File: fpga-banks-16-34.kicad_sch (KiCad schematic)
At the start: 25 parts, among them U1 ASFLMB-100.000MHZ-XY-T, U15 XC7K160T-FFG676, U8 PCA9517ADMR2G

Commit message: Rebase to Rev. 1.2.2
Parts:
- removed C145, C146, C18, C206, C207: C_100n_0402, antmicro-footprints:0402-cap, symbol antmicroCapacitors0402:C_100n_0402
- removed R163: R_10k_0402, data-center-dram-tester-footprints:0402-res, symbol data-center-dram-tester:R_10k_0402
- removed R164, R165, R166, R167, R168, R169: R_0R_0402, data-center-dram-tester-footprints:0402-res, symbol data-center-dram-tester:R_0R_0402
- removed R170, R171, R172, R173, R174: R_4k7_0402, data-center-dram-tester-footprints:0402-res, symbol data-center-dram-tester:R_4k7_0402
- removed R63, R64: R_80R6_0603, antmicro-footprints:0603-res, symbol antmicroResistors0603:R_80R6_0603
- removed R65, R66: R_1k_0603, data-center-dram-tester-footprints:0603-res, symbol data-center-dram-tester:R_1k_0603
- removed TP12: TP_SMD1MM, data-center-dram-tester-footprints:Testpoint_smd_1mm, symbol data-center-dram-tester:TP_SMD1MM
- removed U1: ASFLMB-100.000MHZ-XY-T, data-center-dram-tester-footprints:ASFLMB-100.000MHZ-XY-T, symbol data-center-dram-tester:ASFLMB-100.000MHZ-XY-T
- removed U15: XC7K160T-FFG676, antmicro-footprints:xc7k160tfbg676, symbol data-center-dram-tester:XC7K160T-FFG676
- removed U8: PCA9517ADMR2G, data-center-dram-tester-footprints:TSSOP-8_W3mm, symbol data-center-dram-tester:PCA9517ADMR2G
- added C145, C146, C18, C206, C207: C_100n_0402, data-center-rdimm-ddr4-tester-footprints:C_0402_1005Metric, symbol data-center-rdimm-ddr4-tester:C_100n_0402
- added R163: R_10k_0402, data-center-rdimm-ddr4-tester-footprints:R_0402_1005Metric, symbol data-center-rdimm-ddr4-tester:R_10k_0402
- added R164, R165, R166, R167, R168, R169: R_0R_0402, data-center-rdimm-ddr4-tester-footprints:R_0402_1005Metric, symbol data-center-rdimm-ddr4-tester:R_0R_0402
- added R170, R171, R172, R173, R174: R_4k7_0402, data-center-rdimm-ddr4-tester-footprints:R_0402_1005Metric, symbol data-center-rdimm-ddr4-tester:R_4k7_0402
- added R63, R64: R_80R6_0603, data-center-rdimm-ddr4-tester-footprints:R_0603_1608Metric, symbol data-center-rdimm-ddr4-tester:R_80R6_0603
- added R65, R66: R_1k_0603, data-center-rdimm-ddr4-tester-footprints:R_0603_1608Metric, symbol data-center-rdimm-ddr4-tester:R_1k_0603
- added TP12: TP_1mm_SMD, data-center-rdimm-ddr4-tester-footprints:Testpoint_smd_1mm, symbol data-center-rdimm-ddr4-tester:TP_1mm_SMD
- added U1: Oscillator_SMD_100MHz_ASFLMB, data-center-rdimm-ddr4-tester-footprints:Oscillator_SMD_Abracon_ASFLMB_5x3.2x0.85mm, symbol data-center-rdimm-ddr4-tester:Oscillator_SMD_100MHz_ASFLMB
- added U15: XC7K160T-FFG676, data-center-rdimm-ddr4-tester-footprints:BGA-676_27x27mm_Layout26x26_P1X1mm, symbol data-center-rdimm-ddr4-tester:XC7K160T-FFG676
- added U8: PCA9517A_TSSOP, data-center-rdimm-ddr4-tester-footprints:TSSOP-8_3x3mm_P0.65mm, symbol data-center-rdimm-ddr4-tester:PCA9517A_TSSOP
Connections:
- net 3V3_SYS: now also C145.1, C206.1, R171.1, R172.1, U1.1 (~{STDB}), U1.4 (V_{DD}), U15.A11 (VCCO_16), U15.B8 (VCCO_16), U15.C15 (VCCO_16), U15.D12 (VCCO_16), U15.E9 (VCCO_16), U15.G13 (VCCO_16), U15.H10 (VCCO_16), U8.8 (VREF_{2})
- net A0: now also U15.AF10 (IO_L24P_T3_33)
- net A1: now also U15.AC11 (IO_L13N_T2_MRCC_33)
- net A10\AP: now also U15.Y12 (IO_L18N_T2_33)
- net A11: now also U15.AB7 (IO_L10P_T1_33)
- net A12\~{BC}: now also U15.AC7 (IO_L10N_T1_33)
- net A13: now also U15.AD13 (IO_L17N_T2_33)
- net A17: now also U15.AC13 (IO_L17P_T2_33)
- net A2: now also U15.AD11 (IO_L19P_T3_33)
- net A3: now also U15.AD10 (IO_L20P_T3_33)
- net A4: now also U15.AC9 (IO_L12P_T1_MRCC_33)
- net A5: now also U15.AD9 (IO_L12N_T1_MRCC_33)
- net A6: now also U15.AB9 (IO_L11N_T1_SRCC_33)
- net A7: now also U15.AF7 (IO_L7N_T1_33)
- net A8: now also U15.AE8 (IO_L22P_T3_33)
- net A9: now also U15.AE7 (IO_L7P_T1_33)
- net BA0: now also U15.AB11 (IO_L13P_T2_MRCC_33)
- net BA1: now also U15.AB10 (IO_L14N_T2_SRCC_33)
- net BG0: now also U15.AA9 (IO_L11P_T1_SRCC_33)
- net BG1: now also U15.AF9 (IO_L24N_T3_33)
- net CK0_N: now also U15.AF12 (IO_L21N_T3_DQS_33)
- net CK0_P: now also U15.AE12 (IO_L21P_T3_DQS_33)
- net CK1_N: now also U15.AC12 (IO_L15N_T2_DQS_33)
- net CK1_P: now also U15.AB12 (IO_L15P_T2_DQS_33)
- net CKE0: now also U15.AA8 (IO_L8P_T1_33)
- net CKE1\NC: now also U15.AA7 (IO_L8N_T1_33)
- net DQ0: now also U15.U5 (IO_L1N_T0_34)
- net DQ1: now also U15.V6 (IO_L5N_T0_34)
- net DQ10: now also U15.AC3 (IO_L14N_T2_SRCC_34)
- net DQ11: now also U15.AC4 (IO_L14P_T2_SRCC_34)
- net DQ12: now also U15.W4 (IO_L6N_T0_VREF_34)
- net DQ13: now also U15.V4 (IO_L6P_T0_34)
- net DQ14: now also U15.AA4 (IO_L13P_T2_MRCC_34)
- net DQ15: now also U15.AB4 (IO_L13N_T2_MRCC_34)
- net DQ16: now also U15.V1 (IO_L8N_T1_34)
- net DQ17: now also U15.Y2 (IO_L7N_T1_34)
- net DQ18: now also U15.AC2 (IO_L11N_T1_SRCC_34)
- net DQ19: now also U15.AE1 (IO_L20N_T3_34)
- net DQ2: now also U15.AB6 (IO_L16P_T2_34)
- net DQ20: now also U15.U1 (IO_L2N_T0_34)
- net DQ21: now also U15.V2 (IO_L8P_T1_34)
- net DQ22: now also U15.AB2 (IO_L11P_T1_SRCC_34)
- net DQ23: now also U15.AD1 (IO_L20P_T3_34)
- net DQ24: now also U15.AE3 (IO_L22P_T3_34)
- net DQ25: now also U15.AF3 (IO_L24P_T3_34)
- net DQ26: now also U15.AD5 (IO_L18N_T2_34)
- net DQ27: now also U15.AD6 (IO_L18P_T2_34)
- net DQ28: now also U15.AE2 (IO_L22N_T3_34)
- net DQ29: now also U15.AF2 (IO_L24N_T3_34)
- net DQ3: now also U15.AC6 (IO_L16N_T2_34)
- net DQ30: now also U15.AE5 (IO_L23N_T3_34)
- net DQ31: now also U15.AE6 (IO_L23P_T3_34)
- net DQ32: now also U15.AF15 (IO_L2N_T0_32)
- net DQ33: now also U15.AE16 (IO_L6N_T0_VREF_32)
- net DQ34: now also U15.AF19 (IO_L5P_T0_32)
- net DQ35: now also U15.AF20 (IO_L5N_T0_32)
- net DQ36: now also U15.AF14 (IO_L2P_T0_32)
- net DQ37: now also U15.AD14 (IO_L8N_T1_32)
- net DQ38: now also U15.AF18 (IO_L3N_T0_DQS_32)
- net DQ39: now also U15.AE18 (IO_L3P_T0_DQS_32)
- net DQ4: now also U15.U7 (IO_L5P_T0_34)
- net DQ40: now also U15.AB14 (IO_L10P_T1_32)
- net DQ41: now also U15.AD19 (IO_L17N_T2_32)
- net DQ42: now also U15.AC16 (IO_L12N_T1_MRCC_32)
- net DQ43: now also U15.AB15 (IO_L10N_T1_32)
- net DQ44: now also U15.AC14 (IO_L8P_T1_32)
- net DQ45: now also U15.AD16 (IO_L6P_T0_32)
- net DQ46: now also U15.AC19 (IO_L17P_T2_32)
- net DQ47: now also U15.AC17 (IO_L14N_T2_SRCC_32)
- net DQ48: now also U15.AA15 (IO_L7N_T1_32)
- net DQ49: now also U15.AB17 (IO_L14P_T2_SRCC_32)
- net DQ5: now also U15.U6 (IO_L1P_T0_34)
- net DQ50: now also U15.AA19 (IO_L16P_T2_32)
- net DQ51: now also U15.AA20 (IO_L16N_T2_32)
- net DQ52: now also U15.AA14 (IO_L7P_T1_32)
- net DQ53: now also U15.AB16 (IO_L12P_T1_MRCC_32)
- net DQ54: now also U15.AB19 (IO_L18P_T2_32)
- net DQ55: now also U15.AB20 (IO_L18N_T2_32)
- net DQ56: now also U15.V14 (IO_L24P_T3_32)
- net DQ57: now also U15.Y16 (IO_L9N_T1_DQS_32)
- net DQ58: now also U15.W19 (IO_L21N_T3_DQS_32)
- net DQ59: now also U15.V19 (IO_L23N_T3_32)
- net DQ6: now also U15.AA5 (IO_L15P_T2_DQS_34)
- net DQ60: now also U15.W14 (IO_L24N_T3_32)
- net DQ61: now also U15.Y15 (IO_L9P_T1_DQS_32)
- net DQ62: now also U15.W18 (IO_L21P_T3_DQS_32)
- net DQ63: now also U15.V18 (IO_L23P_T3_32)
- net DQ7: now also U15.AB5 (IO_L15N_T2_DQS_34)
- net DQ8: now also U15.U2 (IO_L2P_T0_34)
- net DQ9: now also U15.Y3 (IO_L7P_T1_34)
- net DQS0_N: now also U15.Y5 (IO_L17N_T2_34)
- net DQS0_P: now also U15.Y6 (IO_L17P_T2_34)
- net DQS10_N: now also U15.W3 (IO_L4N_T0_34)
- net DQS10_P: now also U15.V3 (IO_L4P_T0_34)
- net DQS11_N: now also U15.Y1 (IO_L10N_T1_34)
- net DQS11_P: now also U15.W1 (IO_L10P_T1_34)
- net DQS12_N: now also U15.AD3 (IO_L19N_T3_VREF_34)
- net DQS12_P: now also U15.AD4 (IO_L19P_T3_34)
- net DQS13_N: now also U15.AE15 (IO_L4N_T0_32)
- net DQS13_P: now also U15.AD15 (IO_L4P_T0_32)
- net DQS14_N: now also U15.AE20 (IO_L15N_T2_DQS_32)
- net DQS14_P: now also U15.AD20 (IO_L15P_T2_DQS_32)
- net DQS15_N: now also U15.AA18 (IO_L11N_T1_SRCC_32)
- net DQS15_P: now also U15.AA17 (IO_L11P_T1_SRCC_32)
- net DQS16_N: now also U15.W16 (IO_L22N_T3_32)
- net DQS16_P: now also U15.W15 (IO_L22P_T3_32)
- net DQS1_N: now also U15.AA2 (IO_L12N_T1_MRCC_34)
- net DQS1_P: now also U15.AA3 (IO_L12P_T1_MRCC_34)
- net DQS2_N: now also U15.AC1 (IO_L9N_T1_DQS_34)
- net DQS2_P: now also U15.AB1 (IO_L9P_T1_DQS_34)
- net DQS3_N: now also U15.AF4 (IO_L21N_T3_DQS_34)
- net DQS3_P: now also U15.AF5 (IO_L21P_T3_DQS_34)
- net DQS4_N: now also U15.AF17 (IO_L1N_T0_32)
- net DQS4_P: now also U15.AE17 (IO_L1P_T0_32)
- net DQS5_N: now also U15.AD18 (IO_L13N_T2_MRCC_32)
- net DQS5_P: now also U15.AC18 (IO_L13P_T2_MRCC_32)
- net DQS6_N: now also U15.Y18 (IO_L19N_T3_VREF_32)
- net DQS6_P: now also U15.Y17 (IO_L19P_T3_32)
- net DQS7_N: now also U15.V17 (IO_L20N_T3_32)
- net DQS7_P: now also U15.V16 (IO_L20P_T3_32)
- net DQS9_N: now also U15.W5 (IO_L3N_T0_DQS_34)
- net DQS9_P: now also U15.W6 (IO_L3P_T0_DQS_34)
- net GCLK100: now also U1.3 (OUT), U15.C12 (IO_L13P_T2_MRCC_16)
- net GND: now also C145.2, C146.2, C18.2, C206.2, C207.2, R165.2, R167.2, R169.2, R64.2, R66.2, U1.2 (GND), U8.4 (GND)
- net NC\C2: now also U15.W10 (IO_L3P_T0_DQS_33)
- net ODT0: now also U15.Y13 (IO_L18P_T2_33)
- net ODT1\NC: now also U15.W9 (IO_L3N_T0_DQS_33)
- net PARITY: now also U15.AE13 (IO_L23P_T3_33)
- net SA0: now also R168.2, R169.1
- net SA1: now also R166.2, R167.1
- net SA2: now also R164.2, R165.1
- net SCL_2V5: now also R174.2, U8.2 (SCL_{1})
- net SCL_3V3: now also R171.2, U8.7 (SCL_{2})
- net SDA_2V5: now also R173.2, U8.3 (SDA_{1})
- net SDA_3V3: now also R172.2, U8.6 (SDA_{2})
- net SD_CD: now also U15.F9 (IO_L7P_T1_16)
- net SD_CLK: now also U15.D10 (IO_L12N_T1_MRCC_16)
- net SD_CMD: now also U15.D8 (IO_L8N_T1_16)
- net SD_DAT0: now also U15.E10 (IO_L12P_T1_MRCC_16)
- net SD_DAT1: now also U15.F8 (IO_L7N_T1_16)
- net SD_DAT2: now also U15.C9 (IO_L10P_T1_16)
- net SD_DAT3: now also U15.D9 (IO_L8P_T1_16)
- net TMDS_CLK_N: now also U15.A15 (IO_L23N_T3_16)
- net TMDS_CLK_P: now also U15.B15 (IO_L23P_T3_16)
- net TMDS_D0_N: now also U15.A14 (IO_L21N_T3_DQS_16)
- net TMDS_D0_P: now also U15.B14 (IO_L21P_T3_DQS_16)
- net TMDS_D1_N: now also U15.A12 (IO_L24N_T3_16)
- net TMDS_D1_P: now also U15.A13 (IO_L24P_T3_16)
- net TMDS_D2_N: now also U15.A10 (IO_L22N_T3_16)
- net TMDS_D2_P: now also U15.B10 (IO_L22P_T3_16)
- net VDDQ: now also R170.1, R63.2, R65.1, U15.AA1 (VCCO_34), U15.AA11 (VCCO_33), U15.AB18 (VCCO_32), U15.AB8 (VCCO_33), U15.AC15 (VCCO_32), U15.AC5 (VCCO_34), U15.AD12 (VCCO_33), U15.AD2 (VCCO_34), U15.AE19 (VCCO_32), U15.AE9 (VCCO_33), U15.AF16 (VCCO_32), U15.AF6 (VCCO_34), U15.U3 (VCCO_34), U15.V10 (VCCO_33), U15.W17 (VCCO_32), U15.W7 (VCCO_33), U15.Y14 (VCCO_32), U15.Y4 (VCCO_34)
- net VDDSPD: now also C207.1, R164.1, R166.1, R168.1, R173.1, R174.1, U8.1 (VREF_{1})
- net VREF_33: now also C146.1, C18.1, R65.2, R66.1, U15.AE11 (IO_L19N_T3_VREF_33)
- net VRN: now also R63.1, U15.U9 (IO_0_VRN_33)
- net VRP: now also R64.1, U15.V12 (IO_25_VRP_33)
- net ~{ACT}: now also U15.Y8 (IO_L4P_T0_33)
- net ~{ALERT}: now also U15.AE10 (IO_L20N_T3_33)
- net ~{CAS}\A15: now also U15.AF13 (IO_L23N_T3_33)
- net ~{CS0}: now also U15.V9 (IO_L6P_T0_33)
- net ~{CS1}\NC: now also U15.Y11 (IO_L5P_T0_33)
- net ~{CS2}\C0: now also U15.V11 (IO_L1P_T0_33)
- net ~{CS3}\C1,NC: now also U15.W11 (IO_L1N_T0_33)
- net ~{EVENT}: now also R163.2, R170.2
- net ~{PERST}: now also U15.A8 (IO_L9N_T1_DQS_16)
- net ~{RAS}\A16: now also U15.AA12 (IO_L16N_T2_33)
- net ~{RESET}: now also U15.AF8 (IO_L22N_T3_33)
- net ~{SAVE}: now also U15.Y10 (IO_L5N_T0_33)
- net ~{WE}\A14: now also U15.AA13 (IO_L16P_T2_33)
- new net: R163.1, U15.Y7 (IO_L4N_T0_33)
- new net: TP12.1, U8.5 (EN)
- no-connect marks 0 -> 43

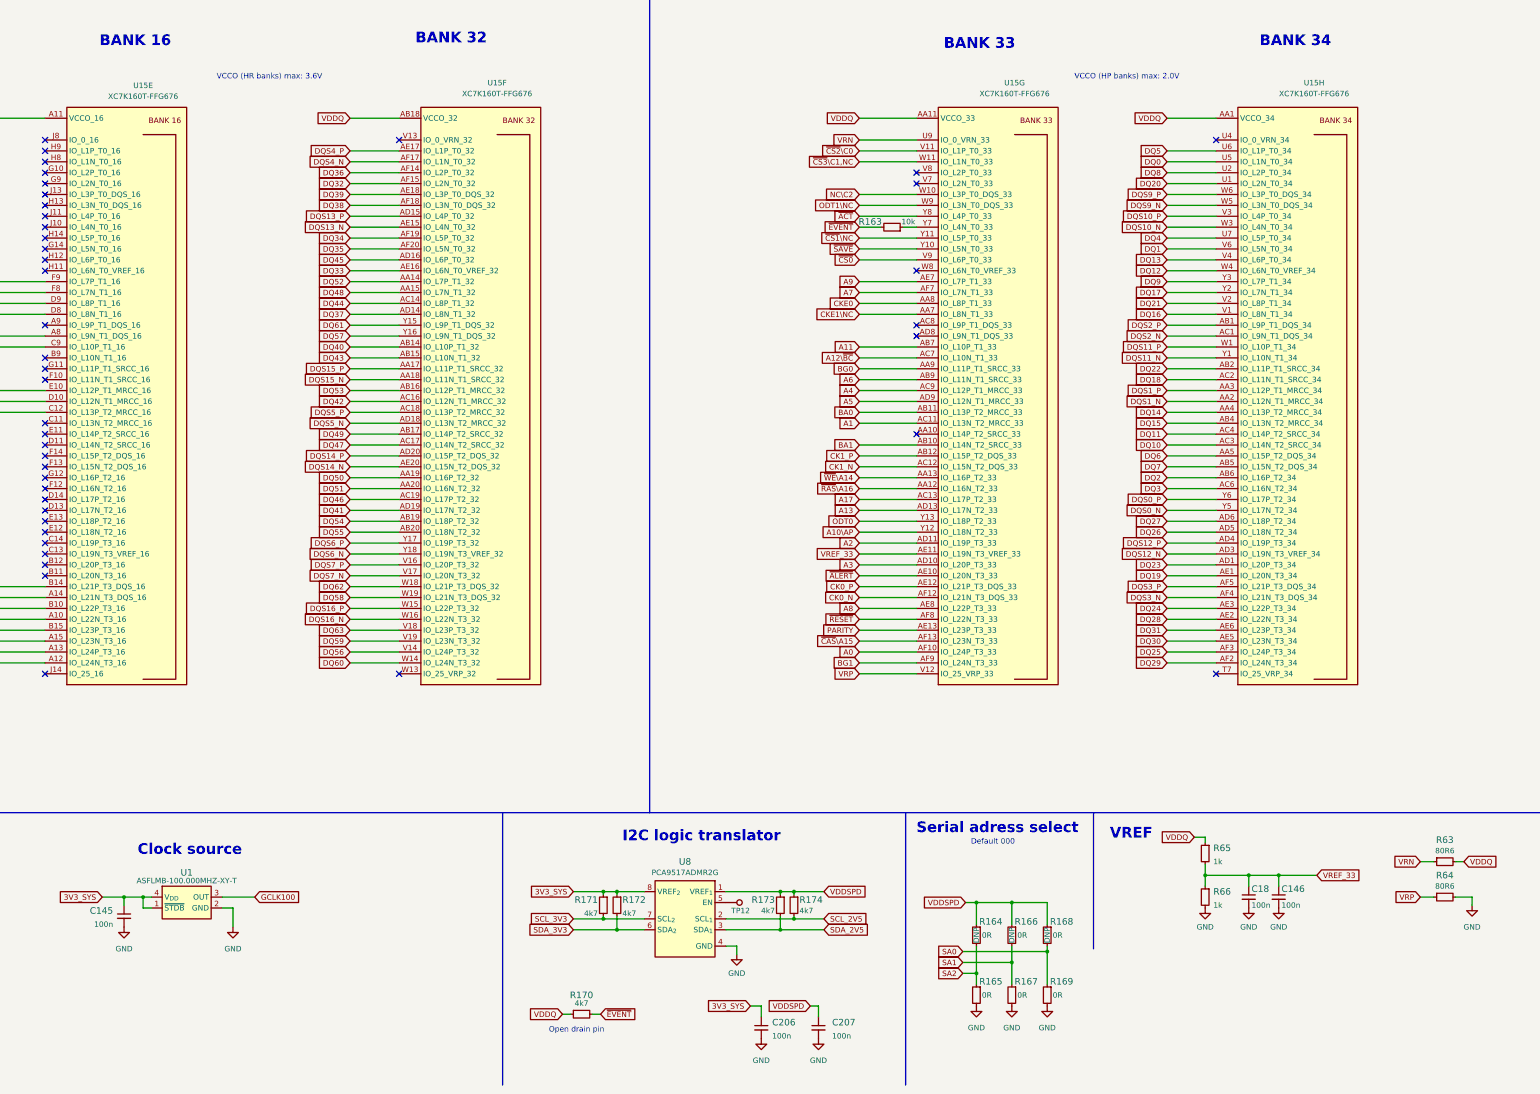
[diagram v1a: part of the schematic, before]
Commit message: Update designators and sync schematic with PCB
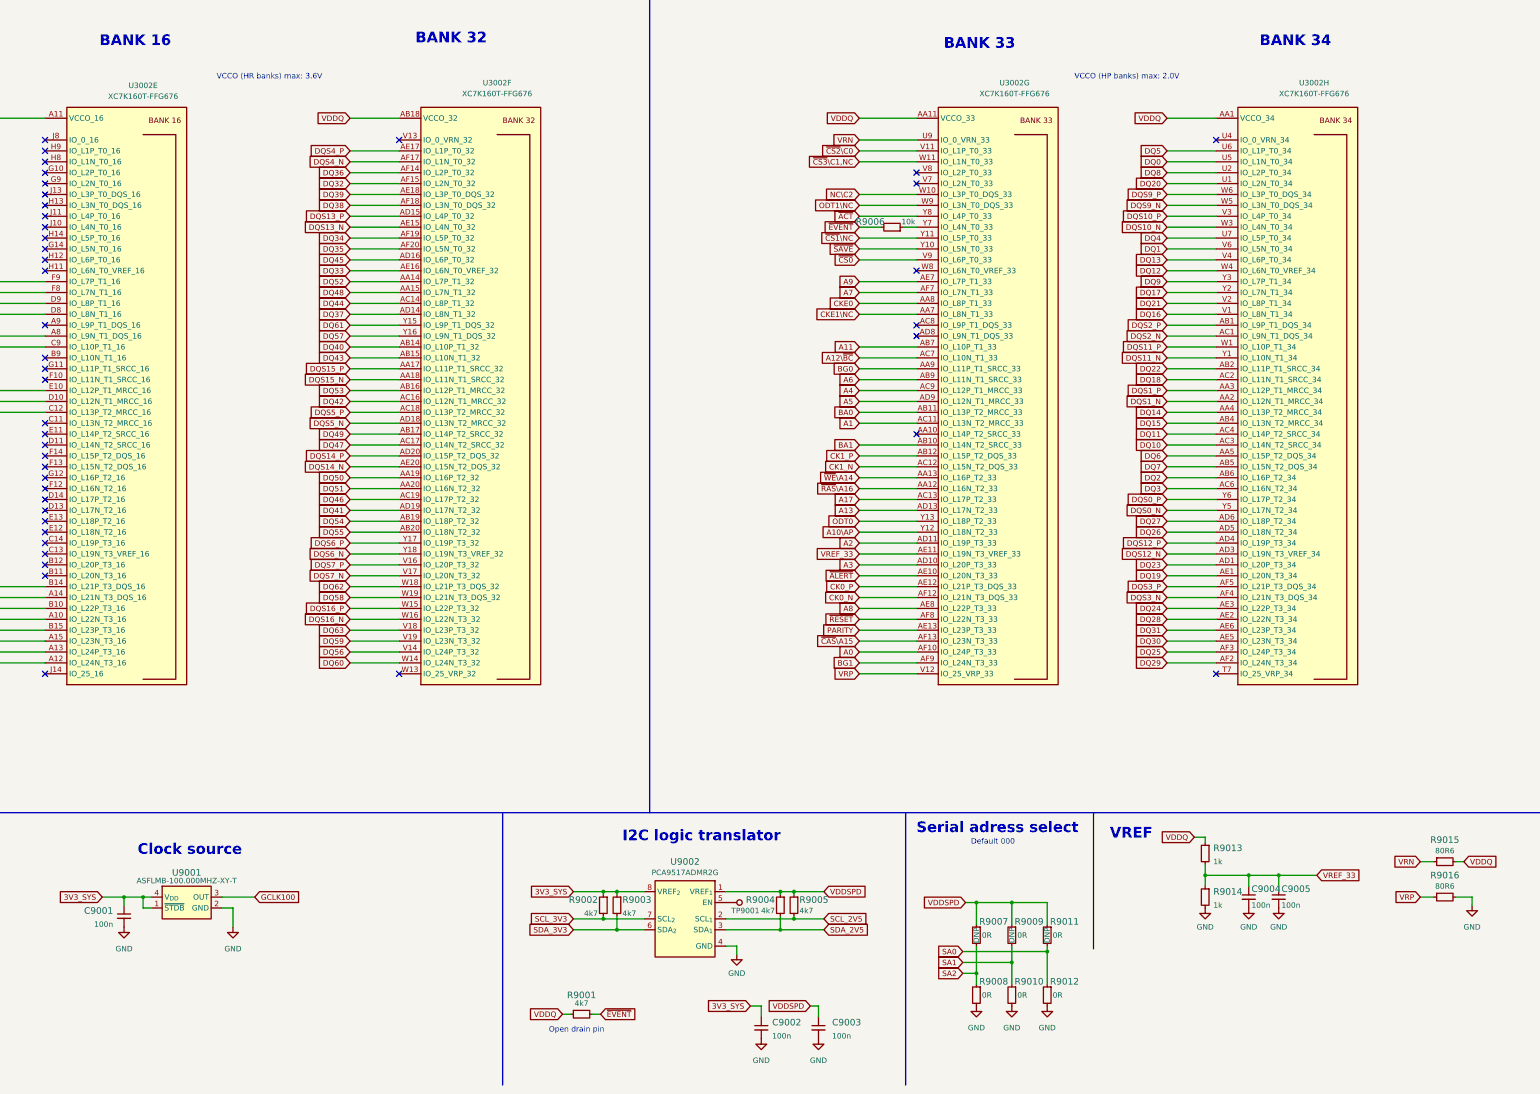
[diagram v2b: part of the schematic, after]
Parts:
- renumbered C145 to C9001, C206 to C9002, C207 to C9003, C18 to C9004, C146 to C9005, R170 to R9001, R171 to R9002, R172 to R9003, R173 to R9004, R174 to R9005, R163 to R9006, R164 to R9007, R165 to R9008, R166 to R9009, R167 to R9010, R168 to R9011, R169 to R9012, R65 to R9013, R66 to R9014, R63 to R9015, R64 to R9016, TP12 to TP9001, U15 to U3002, U1 to U9001, U8 to U9002
